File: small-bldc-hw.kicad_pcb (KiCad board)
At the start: 2 copper layers, 98 parts, among them J1 More IO, J2 TEMP, J3 CONN_01X01, J4 CONN_01X01, J5 CONN_01X01, J6 CAN, J7 I2C, J8 CONN_01X01, J9 CONN_01X01, P2 SWD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

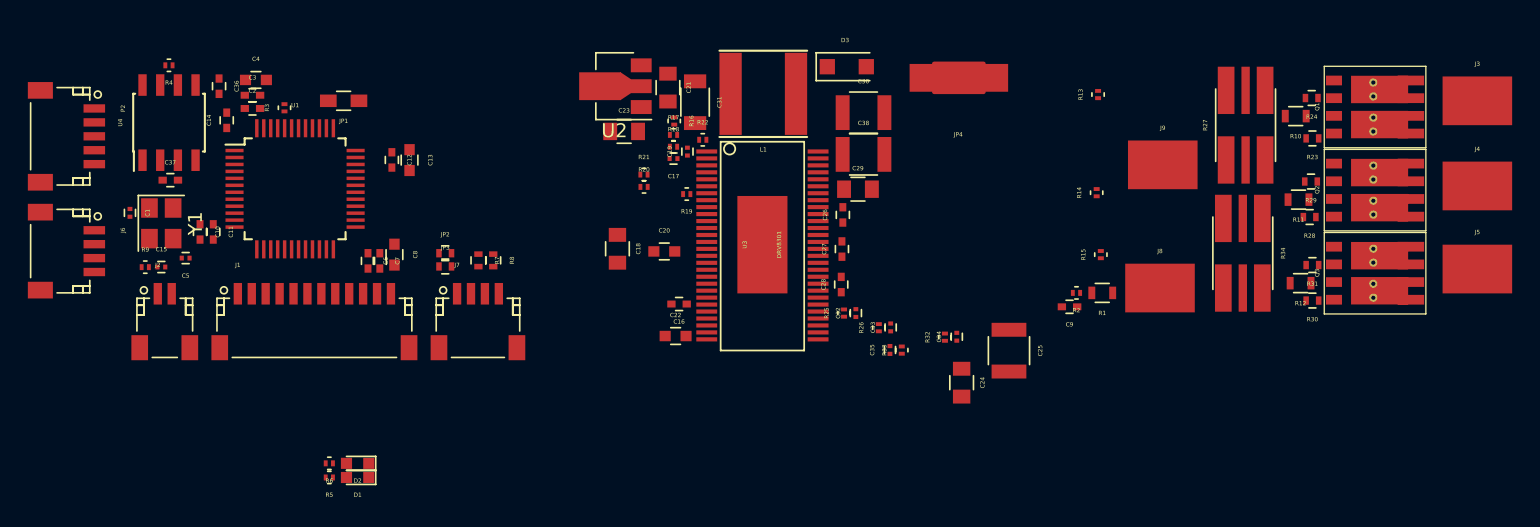
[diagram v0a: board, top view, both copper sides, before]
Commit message: routed parts of the power section
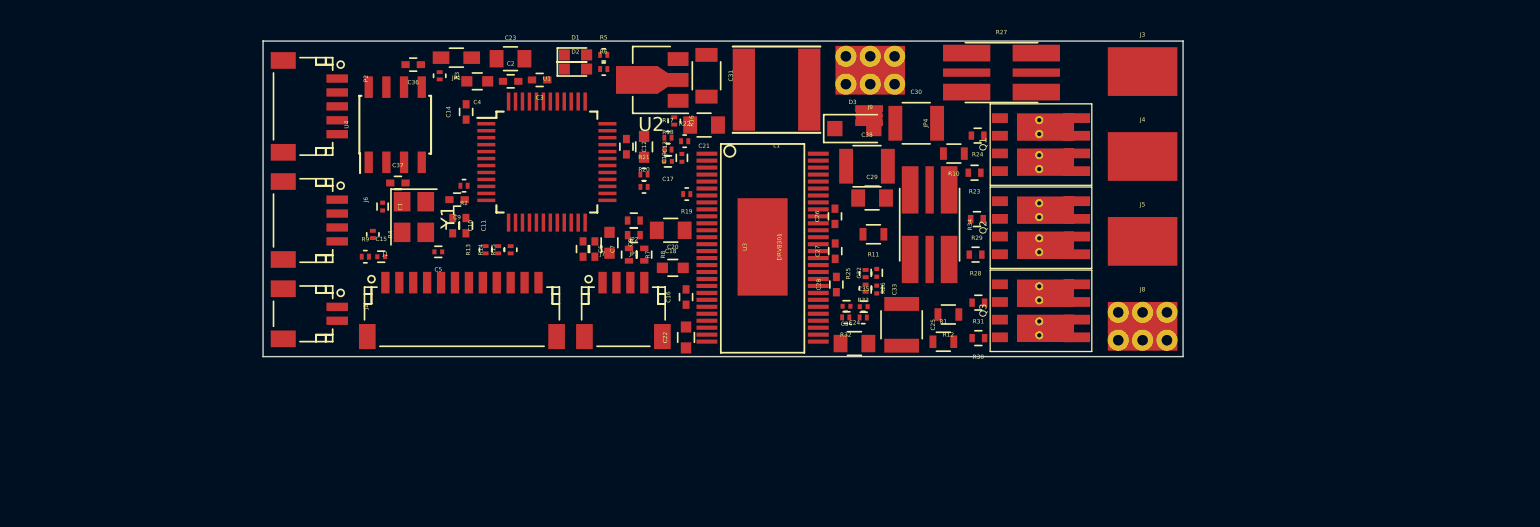
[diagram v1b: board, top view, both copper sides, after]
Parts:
- J8, J9: footprint hlib:SolderWirePad_single_SMD_5x3.5mm -> hlib:SolderWirePad_single_SMD_5x3.5mm_holes
- JP4: footprint Oddities:NetTie-I_Connected_SMD -> hlib:NetTie-I_Connected_SMD
- Q1, Q2, Q3: footprint hlib:SOT-1205 -> hlib:SOT-1205_open_vias
- U2: value AZ1117CH-3.3TRG1 -> AZ1117C
- Y1: footprint Crystals:Crystal_SMD_3225-4pin_3.2x2.5mm -> hlib:Crystal_SMD_3225-4pin_3.2x2.5mm
- moved R13 45.4 mm to (134.8, 104.4)
- moved C9 44.7 mm to (132.8, 100.8)
- moved R2 44.7 mm to (133.2, 99.8)
- moved R14 43.2 mm to (135.7, 104.4)
- moved R15 42.4 mm to (136.6, 104.4)
- moved R5 36.2 mm to (143.3, 90.4), turned to 0 degrees
- moved R6 34.5 mm to (143.3, 91.4), turned to 0 degrees
- moved D1 34.2 mm to (141.3, 90.4), turned to 0 degrees
- moved D2 32.4 mm to (141.3, 91.4), turned to 0 degrees
- moved R11 30.6 mm to (162.7, 103.3)
- moved R12 25.4 mm to (168.0, 109.1)
- moved R10 24.7 mm to (168.4, 97.5)
- moved R23 24.4 mm to (169.9, 98.9)
- moved Q2 24.2 mm to (174.3, 102.8)
- moved Q3 24.2 mm to (174.3, 108.8)
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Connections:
- C30 pad 2: GND -> GNDPWR
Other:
- board outline added: 66.1 x 22.7 mm
- net class Default: clearance 0.2 -> 0.15367; trace_width 0.25 -> 0.1524; via_dia 0.6 -> 0.6858; via_drill 0.4 -> 0.3302
- net class bigpower added: clearance 0.19558, trace_width 1.27, via_dia 1.27, via_drill 0.508
- net class smallpower added: clearance 0.15367, trace_width 0.4572, via_dia 0.6858, via_drill 0.3302
- rule trace_clearance: 0.2 -> 0.15367
- rule trace_min: 0.2 -> 0.1524
- rule via_min_drill: 0.3 -> 0.3302
- rule via_min_size: 0.4 -> 0.508

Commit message: stuff
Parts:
- J3, J4, J5: footprint hlib:SolderWirePad_single_SMD_5x3.5mm -> hlib:SolderWirePad_single_SMD_5x3.5mm_holes
- moved R1 23.5 mm to (146.6, 100.4), turned to 90 degrees
- moved R10 20.6 mm to (148.0, 100.2), turned to 90 degrees
- moved R21 13.4 mm to (132.9, 97.0)
- moved R20 12.4 mm to (134.0, 97.7)
- moved C37 9.28 mm to (129.4, 90.4), turned to 180 degrees
- moved C36 8.65 mm to (127.1, 99.4), turned to 270 degrees
- moved C23 6.52 mm to (143.0, 91.8), turned to 90 degrees
- moved C10 2.87 mm to (133.6, 100.0), turned to 180 degrees
- moved D1 2.11 mm to (139.2, 90.7)
- moved R6 2.06 mm to (141.3, 91.7)
- moved R5 2.06 mm to (141.3, 90.7)
- moved D2 2.06 mm to (139.2, 91.7)
- moved C3 2.04 mm to (136.6, 92.0)
- moved R3 2.04 mm to (133.5, 92.4)
- moved R2 2.02 mm to (133.6, 101.8)
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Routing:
- net GND: track 0.00 -> 237.7 mm, vias 0 -> 29
- net +3V3: track 0.00 -> 137.4 mm, vias 0 -> 12
- net DC_SUPPLY: track 0.00 -> 113.9 mm, vias 0 -> 7
- net +5V: track 0.00 -> 88.1 mm, vias 0 -> 7
- net GNDPWR: track 0.00 -> 70.0 mm, vias 0 -> 4
- net /power/PHASE_A: track 0.00 -> 55.8 mm, vias 0 -> 6
- net /PA7: track 0.00 -> 54.8 mm, vias 0 -> 2
- net /PB0: track 0.00 -> 50.5 mm, vias 0 -> 2
- net /power/PHASE_C: track 0.00 -> 39.4 mm, vias 0 -> 2
- net /PHC_V: track 0.00 -> 38.7 mm, vias 0 -> 2
- net /DRV_OCTW: track 0.00 -> 37.8 mm, vias 0 -> 3
- net /DRV_FAULT: track 0.00 -> 37.1 mm, vias 0 -> 3
- net /PHB_V: track 0.00 -> 37.1 mm, vias 0 -> 2
- net /DRV_DC_CAL: track 0.00 -> 32.5 mm, vias 0 -> 2
- net /power/PHASE_B: track 0.00 -> 32.3 mm, vias 0 -> 3
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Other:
- board size 66.1 x 22.7 mm -> 65 x 22.4 mm
- copper layers 2 -> 4
- net class Default: clearance 0.15367 -> 0.1524
- net class smallpower: clearance 0.15367 -> 0.1524
- rule trace_clearance: 0.15367 -> 0.1524
- rule trace_min: 0.1524 -> 0

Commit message: rerouted a trace
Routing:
- net /DRV_FAULT: track 37.1 -> 28.2 mm
- net /DRV_OCTW: track 37.8 -> 36.9 mm

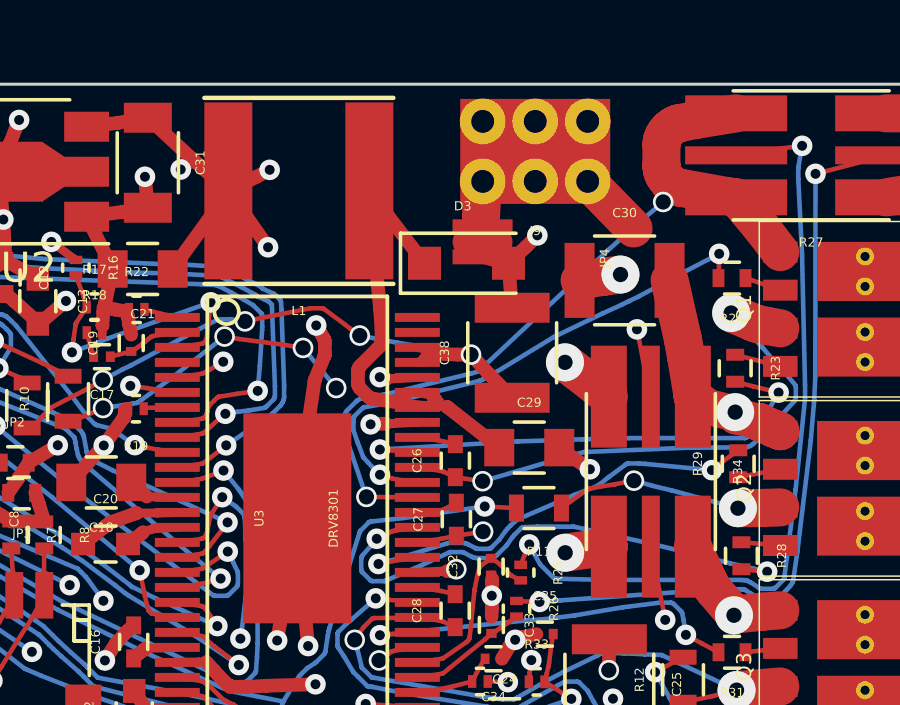
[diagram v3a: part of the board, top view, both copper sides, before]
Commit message: added additional ground via to drv8301 and fixed broken redundant trace
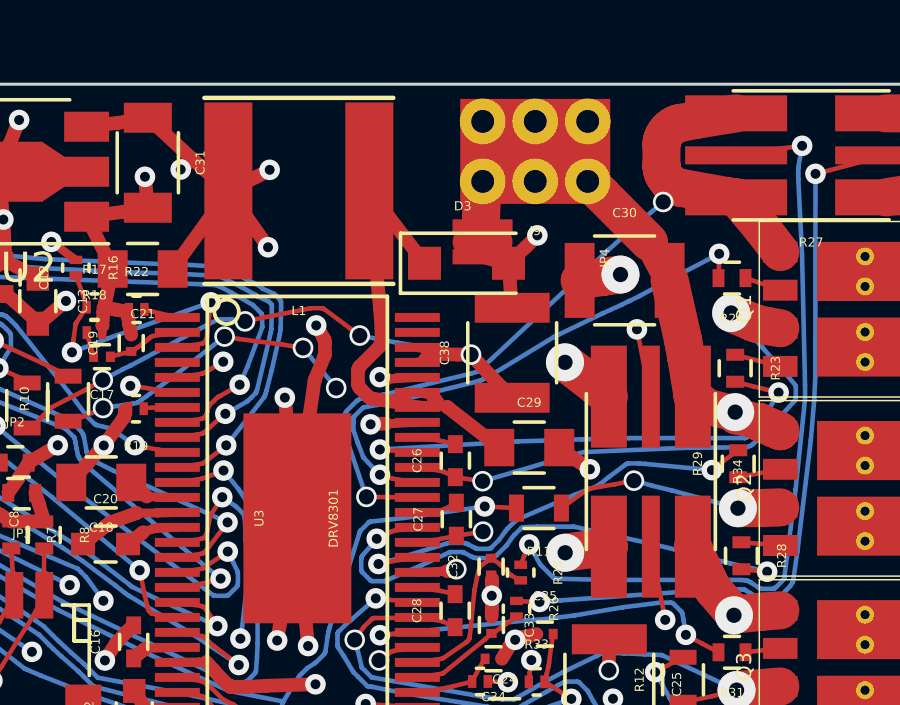
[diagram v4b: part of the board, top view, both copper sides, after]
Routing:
- net GND: track 237.7 -> 241.7 mm, vias 29 -> 30
- net GNDPWR: track 70.0 -> 72.2 mm
- net /MOSI: track 23.5 -> 22.8 mm
- net /DRV_CS: track 19.2 -> 18.6 mm
- net /DRV_OCTW: track 36.9 -> 36.4 mm
